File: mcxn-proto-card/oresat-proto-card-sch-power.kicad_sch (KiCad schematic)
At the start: 89 parts, among them Q1 DMP2110UVTQ-7, Q2 DMPH2040UVTQ-7, Q7 DMPH2040UVTQ-7, Q8 DMN2050LQ-7, Q9 DMN2050LQ-7, U10 TPS62111RSA, U11 MIC842LYC5, U12 MIC842LYC5, U2 MAX7310, U3 TS5A21366DCUR, U6 MAX4211FETE

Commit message: Fix minor details on single part
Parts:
- C18: DPN 490-GRT188R71E105KE13DCT-ND -> 399-C0603C474K3RACAUTOCT-ND; MPN GRT188R71E105KE13D -> C0603C474K3RACAUTO
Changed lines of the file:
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@@
 			)
 		)
-		(property "Description" "1 µF ±10% 25V Ceramic Capacitor X7R 0603 (1608 Metric)"
+		(property "Description" "0.47 µF ±10% 25V Ceramic Capacitor X7R 0603 (1608 Metric)"
 			(at 196.85 50.8 0)
 			(hide yes)
@@
 			)
 		)
-		(property "DPN" "490-GRT188R71E105KE13DCT-ND"
+		(property "DPN" "399-C0603C474K3RACAUTOCT-ND"
 			(at 196.85 50.8 0)
 			(hide yes)
@@
 			)
 		)
-		(property "MPN" "GRT188R71E105KE13D"
+		(property "MPN" "C0603C474K3RACAUTO"
 			(at 196.85 50.8 0)
 			(hide yes)

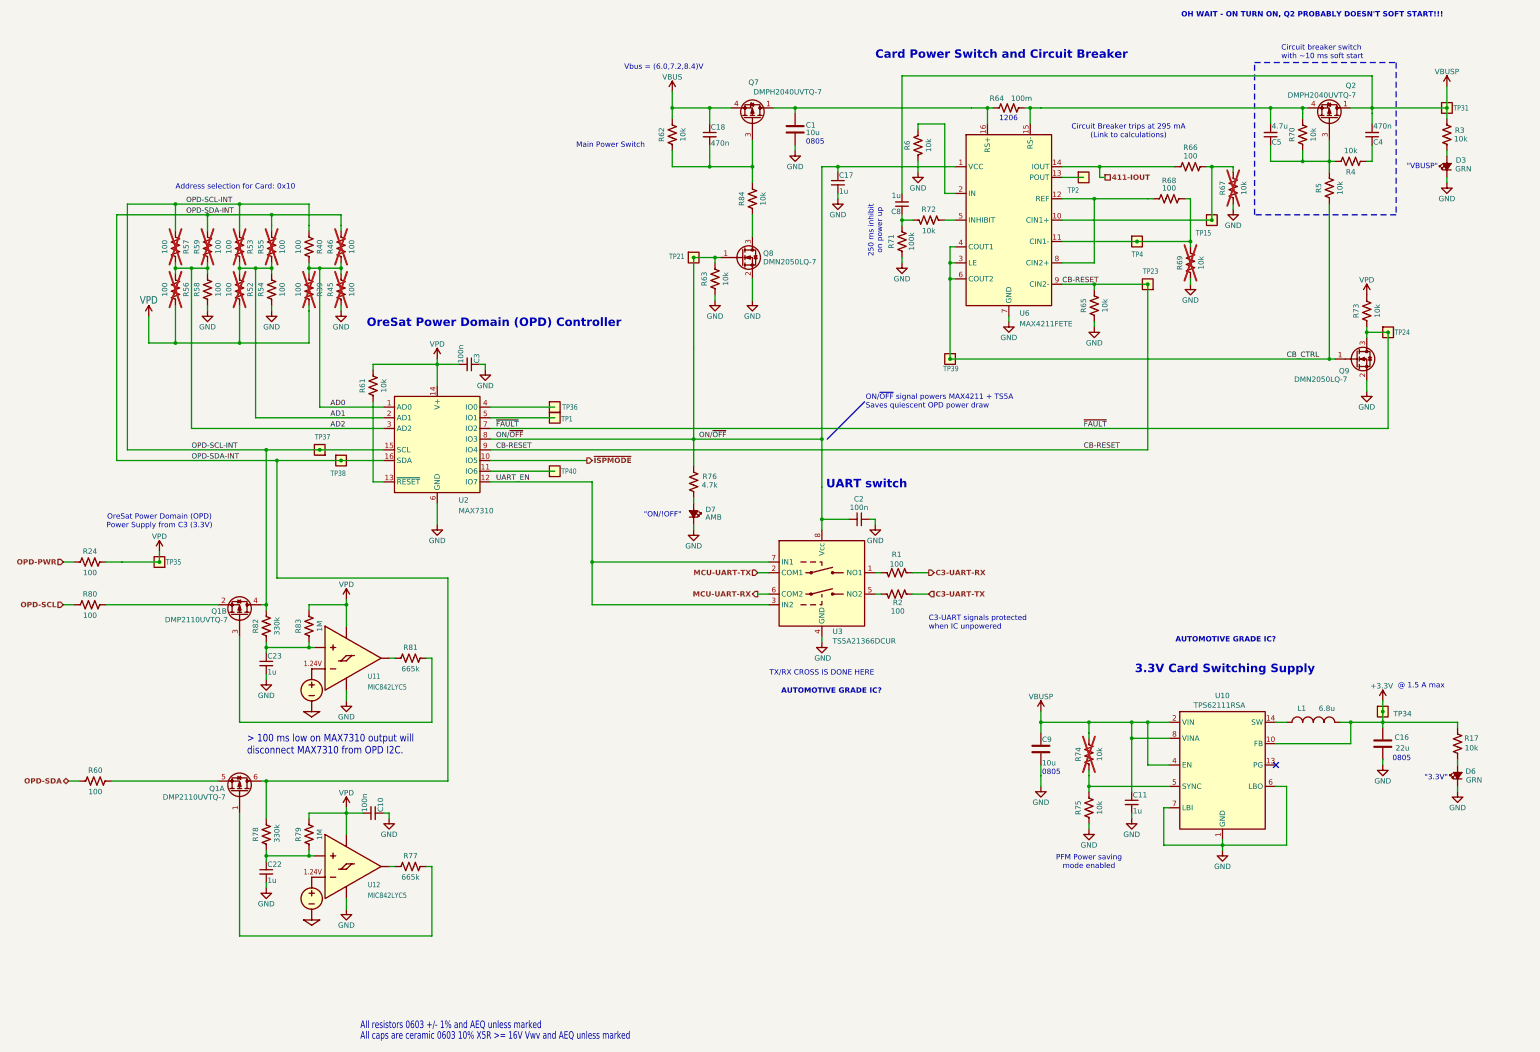
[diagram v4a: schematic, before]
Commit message: Fixed version pins and lots of ref des formatting; BOM still not right.
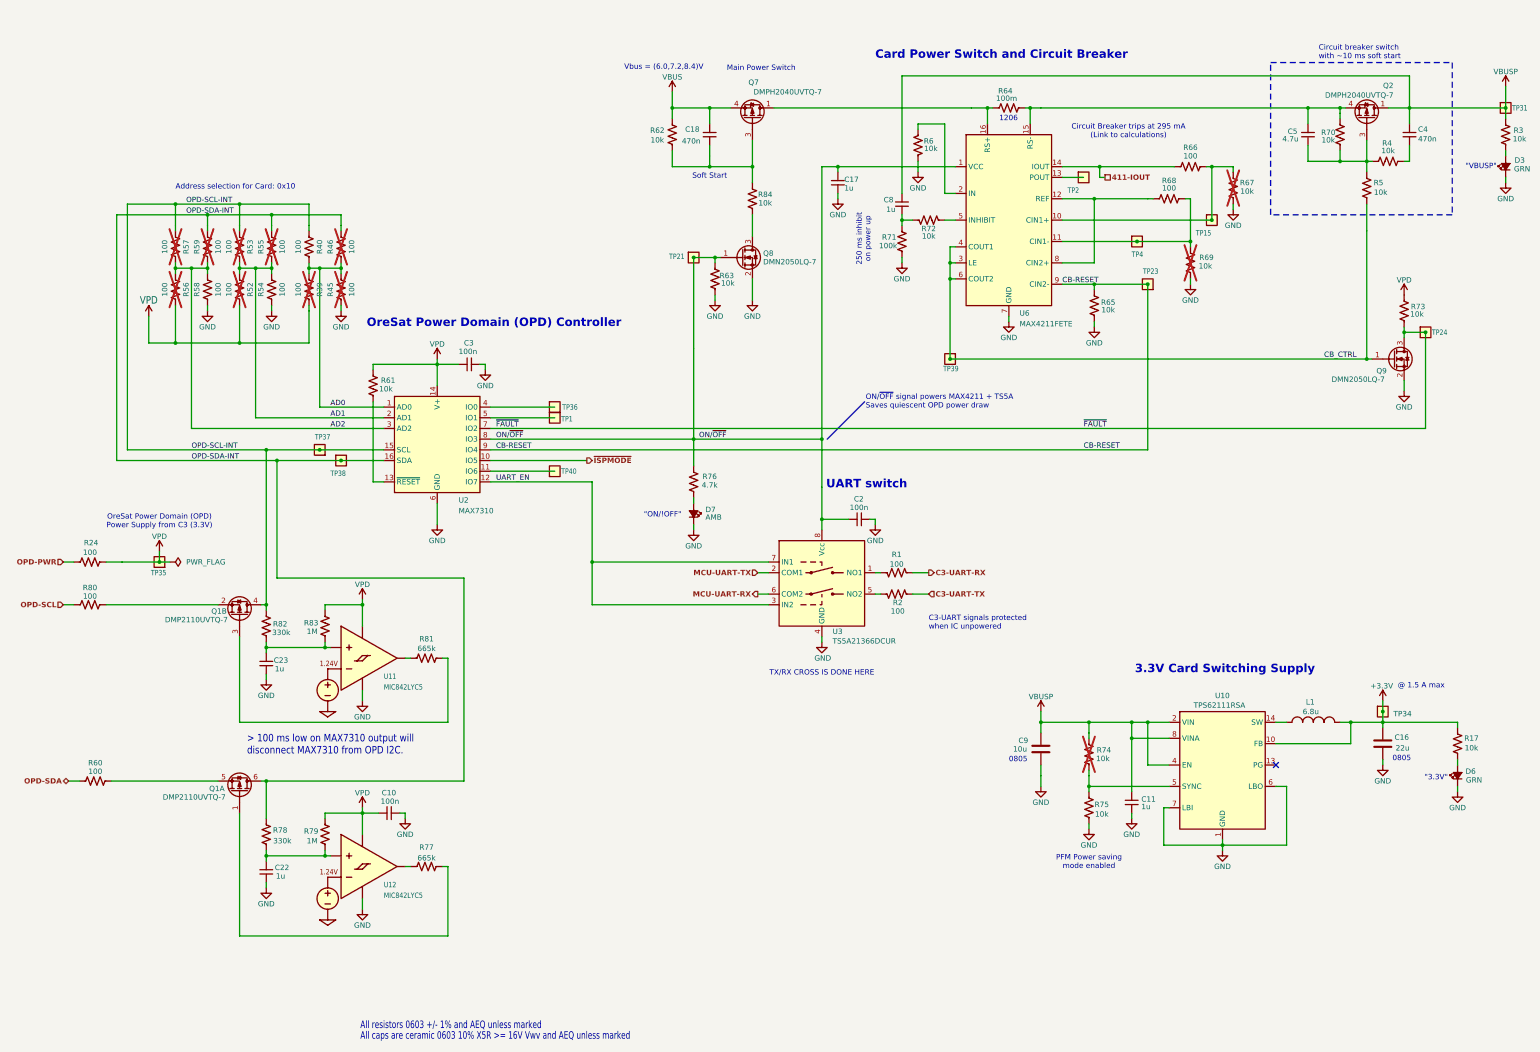
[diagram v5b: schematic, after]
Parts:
- removed C1: 10u, oresat-passives:0805-B-NOSILK, symbol Device:C
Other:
- note added: "Soft Start"
- note removed: "AUTOMOTIVE GRADE IC?"
- note removed: "OH WAIT - ON TURN ON, Q2 PROBABLY DOESN'T SOFT START!!!"
- moved on the sheet: C10, C4, C5, D3, Q2, Q9, R3, R4, R5, R70, R73, R77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

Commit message: Fixed BOM Values
Fixed incorrect component BOM details for C5 and C18
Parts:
- C18: MFR Murata Electronics -> KEMET
- C5: DPN 399-6851-1-ND -> 587-4332-1-ND; MFR KEMET -> Taiyo Yuden; MPN C0603C103K5RACAUTO -> EMK107BBJ475KAHT
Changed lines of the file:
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@@
 			)
 		)
-		(property "Datasheet" "https://search.murata.co.jp/Ceramy/image/img/A01X/G101/ENG/GRT188R71E105KE13-01.pdf"
+		(property "Datasheet" "https://www.yageogroup.com/content/datasheet/asset/file/KEM_C1023_X7R_AUTO_SMD"
 			(at 196.85 50.8 0)
 			(hide yes)
@@
 			)
 		)
-		(property "MFR" "Murata Electronics"
+		(property "MFR" "KEMET"
 			(at 196.85 50.8 0)
 			(hide yes)
@@
 			)
 		)
-		(property "Datasheet" "https://www.yageogroup.com/content/datasheet/asset/file/KEM_C1023_X7R_AUTO_SMD"
+		(property "Datasheet" "https://mm.digikey.com/Volume0/opasdata/d220001/medias/docus/727/EMK107BBJ475KAHT_SS.pdf"
 			(at 339.09 50.8 0)
 			(hide yes)
@@
 			)
 		)
-		(property "Description" "10000 pF ±10% 50V Ceramic Capacitor X7R 0603 (1608 Metric)"
+		(property "Description" "4.7 µF ±10% 16V Ceramic Capacitor X5R 0603 (1608 Metric)"
 			(at 339.09 50.8 0)
 			(hide yes)
@@
 			)
 		)
-		(property "DPN" "399-6851-1-ND"
+		(property "DPN" "587-4332-1-ND"
 			(at 339.09 50.8 0)
 			(hide yes)
@@
 			)
 		)
-		(property "MFR" "KEMET"
+		(property "MFR" "Taiyo Yuden"
 			(at 339.09 50.8 0)
 			(hide yes)
@@
 			)
 		)
-		(property "MPN" "C0603C103K5RACAUTO"
+		(property "MPN" "EMK107BBJ475KAHT"
 			(at 339.09 50.8 0)
 			(hide yes)
